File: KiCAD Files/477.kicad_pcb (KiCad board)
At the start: 2 copper layers, 75 parts, among them IC1 W25N01GVSFIG, IC2 W25N01GVSFIG, IC3 W25N01GVSFIG, IC4 W25N01GVSFIG, IC5 AZ1117IH-3.3TRG1, IC6 USBLC6-2SC6, J1 BM06B-SRSS-TBT_LF__SN_, J2 6364372-2, J3 TSW-103-14-S-D, J4 TSW-103-14-S-D, J5 BM07B-SRSS-TB_LF__SN_, J6 BM09B-SRSS-TB_LF__SN_, J7 TSW-105-05-F-S, U1 STM32H7A3RGTx, Y1 ABM8G-48.000MHZ-18-D2Y-T

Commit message: finished file
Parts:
- moved S1 139.7 mm to (218.2, 129.5)
- moved R10 110.3 mm to (225.8, 102.1)
- moved R9 110.3 mm to (225.8, 104.6)
- moved J3 99.9 mm to (250.4, 45.7)
- moved J1 84.6 mm to (173.7, 130.8)
- moved C12 82.6 mm to (166.9, 128.0), turned to 90 degrees
- moved R13 82.1 mm to (166.9, 131.8), turned to -90 degrees
- moved J7 79.6 mm to (195.6, 131.8), turned to 180 degrees
- moved R7 64.4 mm to (226.0, 109.5)
- moved R5 64.4 mm to (226.0, 114.6)
- moved R6 64.4 mm to (226.0, 112.0)
- moved R8 64.4 mm to (226.0, 106.9)
- moved R4 64.4 mm to (226.0, 117.1)
- moved C19 62.6 mm to (230.6, 100.6)
- moved R17 62.5 mm to (233.4, 100.6)
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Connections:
- IC1 pad 7: PA0/CS1 -> PC9/CS1
- IC1 pad 9: PC2/WP1 -> PC7/WP1
- IC2 pad 1: PC7/HOLD2 -> PC2/HOLD2
- IC2 pad 7: PA1/CS2 -> PC10/CS2
- IC3 pad 1: PC9/HOLD3 -> PC4/HOLD3
- IC3 pad 7: PA2/CS3 -> PA3/CS3
- IC3 pad 9: PC4/WP3 -> PC5/WP3
- IC4 pad 1: PC10/HOLD4 -> PA2/HOLD4
- IC4 pad 7: PA3/CS4 -> PA1/CS4
- IC4 pad 9: PC5/WP4 -> PA0/WP4
- U1 pad 10: PC2/WP1 -> PC2/HOLD2
- U1 pad 14: PA0/CS1 -> PA0/WP4
- U1 pad 15: PA1/CS2 -> PA1/CS4
- U1 pad 16: PA2/CS3 -> PA2/HOLD4
- U1 pad 17: PA3/CS4 -> PA3/CS3
- U1 pad 24: PC4/WP3 -> PC4/HOLD3
- U1 pad 25: PC5/WP4 -> PC5/WP3
- U1 pad 38: PC7/HOLD2 -> PC7/WP1
- U1 pad 39: PC9/HOLD3 -> PC9/CS1
- U1 pad 51: PC10/HOLD4 -> PC10/CS2
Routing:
- net PC1/LCD MOSI: track 0.00 -> 104.4 mm, vias 0 -> 2
- net PB10/LCD SCK: track 0.00 -> 47.9 mm
- net PB12/LCD NSS: track 0.00 -> 37.3 mm, vias 0 -> 2
- net PA0/WP4: track 0.00 -> 35.9 mm, vias 0 -> 2
- net PA3/CS3: track 0.00 -> 34.7 mm, vias 0 -> 2
- net PB13/FP TX: track 0.00 -> 30.5 mm, vias 0 -> 2
- net VBAT: track 0.00 -> 28.7 mm, vias 0 -> 6
- net PD2/FP RX: track 0.00 -> 24.7 mm, vias 0 -> 2
- net PC4/HOLD3: track 0.00 -> 21.4 mm, vias 0 -> 2
- net PC7/WP1: track 0.00 -> 18.3 mm, vias 0 -> 4
- net PA1/CS4: track 0.00 -> 16.7 mm
- net PA6/MISO: track 86.7 -> 103.3 mm, vias 2 -> 4
- net PC6/HOLD1: track 0.00 -> 15.6 mm, vias 0 -> 2
- net PA5/SCK: track 79.4 -> 64.2 mm, vias 3 -> 0
- net PA7/MOSI: track 78.2 -> 65.5 mm, vias 3 -> 2
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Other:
- board outline added: 96 x 57.4 mm
- board text added: "Team 20: Encrypted USB Drive Version: 3/5/2025 2:17 AM"
- board text removed: "Team 20: Encrypted USB Drive Version: 3/1/2025 9:25 PM"

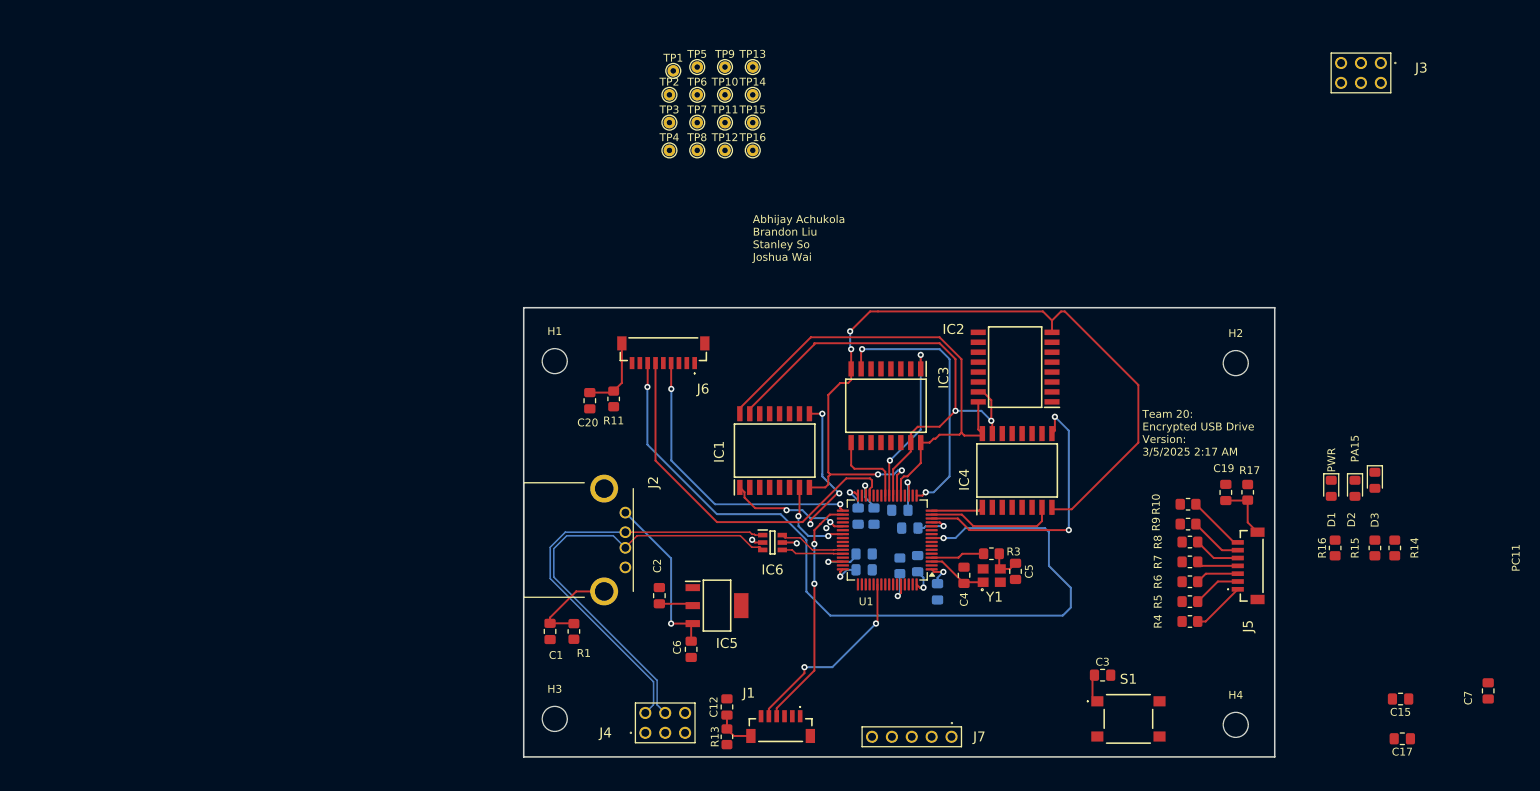
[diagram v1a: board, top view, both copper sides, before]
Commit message: Finalized Signal Routing
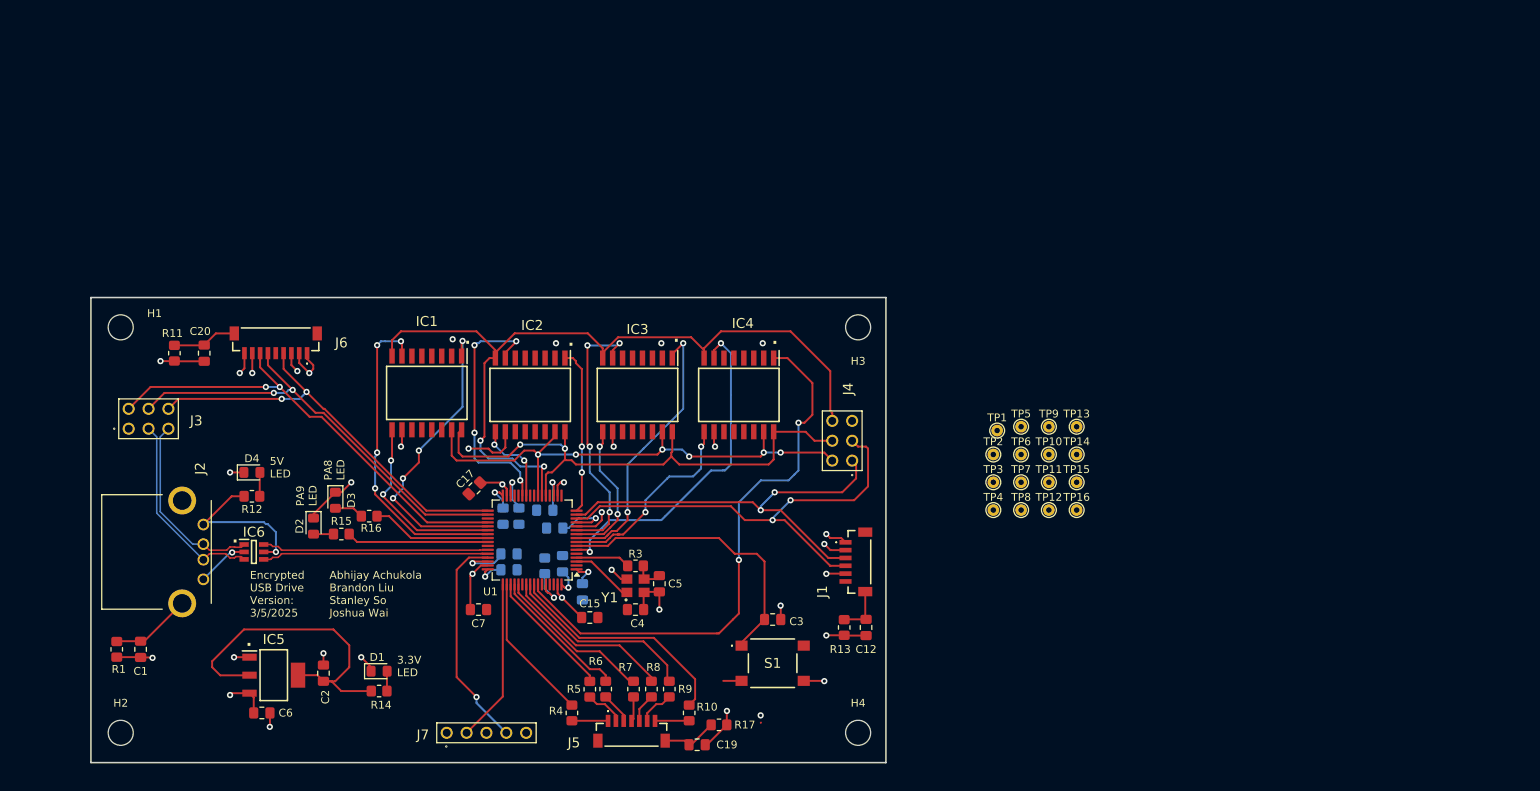
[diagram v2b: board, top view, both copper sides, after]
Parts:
- added D4: LED, LED_SMD:LED_0805_2012Metric_Pad1.15x1.40mm_HandSolder, F.Cu at (106.2, 98.0)
- added R12: 220, Resistor_SMD:R_0805_2012Metric_Pad1.20x1.40mm_HandSolder, F.Cu at (106.2, 101.1)
- moved J3 166.7 mm to (90.4, 92.5), turned to 0 degrees
- moved H2 150.1 mm to (89.4, 131.3)
- moved D2 133.2 mm to (114.0, 104.9)
- moved D3 132.9 mm to (116.8, 101.6)
- moved R15 132.1 mm to (117.6, 105.9), turned to 0 degrees
- moved R14 131.1 mm to (122.4, 126.0), turned to 180 degrees
- moved C7 129.4 mm to (135.1, 115.6), turned to 180 degrees
- moved D1 123.9 mm to (122.4, 123.4), turned to 0 degrees
- moved R16 123.5 mm to (121.2, 103.6), turned to 0 degrees
- moved C17 122.8 mm to (134.6, 100.1), turned to 45 degrees
- moved C15 104.1 mm to (149.4, 116.6)
- moved J5 82.1 mm to (154.7, 131.6), turned to 0 degrees
- moved R4 79.8 mm to (147.1, 128.8), turned to 90 degrees
- moved R5 77.5 mm to (149.4, 125.7), turned to 90 degrees
- moved R6 75.9 mm to (151.4, 125.7), turned to 90 degrees
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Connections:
- IC2 pad 1: PC2/HOLD2 -> PA2/HOLD2
- IC2 pad 7: PC10/CS2 -> PB1/CS2
- IC2 pad 9: PC3/WP2 -> PB0/WP2
- IC3 pad 1: PC4/HOLD3 -> PC1/HOLD3
- IC3 pad 7: PA3/CS3 -> PC3/CS3
- IC3 pad 9: PC5/WP3 -> PC2/WP3
- IC4 pad 1: PA2/HOLD4 -> PB6/HOLD4
- IC4 pad 7: PA1/CS4 -> PH1/CS4
- IC4 pad 9: PA0/WP4 -> PC0/WP4
- J1 pad 2: PC0/Touch Out -> GND
- J1 pad 3: VBAT -> PA1/FP RX
- J1 pad 4: PB13/FP TX -> PA0/FP TX
- J1 pad 5: PD2/FP RX -> VBAT
- J1 pad 6: VBAT -> unconnected-(J1-Pad6)
- J3 pad 2: PA6/MISO -> PB15/LCD MOSI
- J3 pad 3: PB10/LCD SCK -> D+
- J3 pad 4: PA5/SCK -> PB13/LCD SCK
- J3 pad 5: PC1/LCD MOSI -> D-
- J3 pad 6: PA7/MOSI -> PB12/LCD NSS
- J4 pad 1: PC0/Touch Out -> PA1/FP RX
- J4 pad 2: D- -> PA7/MOSI
- J4 pad 3: PB13/FP TX -> PA0/FP TX
- J4 pad 4: D+ -> PA5/SCK
- J4 pad 5: PD2/FP RX -> GND
- J4 pad 6: GND -> PA6/MISO
- J6 pad 6: PB10/LCD SCK -> PB13/LCD SCK
- J6 pad 7: PC1/LCD MOSI -> PB15/LCD MOSI
- R10 pad 1: PB8/KeyC3 -> PB5/KeyC3
- R16 pad 2: PC11/Debug -> PA8/Debug
- R4 pad 2: PB0/KeyR1 -> PA15/KeyR1
- R5 pad 2: PB1/KeyR2 -> PC10/KeyR2
- R6 pad 2: PB2/KeyR3 -> PC11/KeyR3
- R7 pad 1: PB5/KeyR4 -> PC12/KeyR4
- R8 pad 1: PB6/KeyC1 -> PB3/KeyC1
- R9 pad 2: PB7/KeyC2 -> PB4/KeyC2
- TP13 pad 1: PB12/LCD NSS -> unconnected-(TP13-Pad1)
- U1 pad 10: PC2/HOLD2 -> PC2/WP3
- U1 pad 11: PC3/WP2 -> PC3/CS3
- U1 pad 14: PA0/WP4 -> PA0/FP TX
- U1 pad 15: PA1/CS4 -> PA1/FP RX
- U1 pad 16: PA2/HOLD4 -> PA2/HOLD2
- U1 pad 24: PC4/HOLD3 -> unconnected-(U1-PC4-Pad24)
- U1 pad 25: PC5/WP3 -> unconnected-(U1-PC5-Pad25)
- U1 pad 26: PB0/KeyR1 -> PB0/WP2
- U1 pad 27: PB1/KeyR2 -> PB1/CS2
- U1 pad 28: PB2/KeyR3 -> unconnected-(U1-PB2-Pad28)
- U1 pad 29: PB10/LCD SCK -> unconnected-(U1-PB10-Pad29)
- U1 pad 34: PB13/FP TX -> PB13/LCD SCK
- U1 pad 36: unconnected-(U1-PB15-Pad36) -> PB15/LCD MOSI
- U1 pad 40: unconnected-(U1-PA8-Pad40) -> PA8/Debug
- U1 pad 50: unconnected-(U1-PA15-Pad50) -> PA15/KeyR1
- U1 pad 51: PC10/CS2 -> PC10/KeyR2
- U1 pad 52: PC11/Debug -> PC11/KeyR3
- U1 pad 53: unconnected-(U1-PC12-Pad53) -> PC12/KeyR4
- U1 pad 54: PD2/FP RX -> unconnected-(U1-PD2-Pad54)
- U1 pad 55: unconnected-(U1-PB3-Pad55) -> PB3/KeyC1
- U1 pad 56: unconnected-(U1-PB4-Pad56) -> PB4/KeyC2
- U1 pad 57: PB5/KeyR4 -> PB5/KeyC3
- U1 pad 58: PB6/KeyC1 -> PB6/HOLD4
- U1 pad 59: PB7/KeyC2 -> unconnected-(U1-PB7-Pad59)
- U1 pad 6: unconnected-(U1-PH1-Pad6) -> PH1/CS4
- U1 pad 61: PB8/KeyC3 -> unconnected-(U1-PB8-Pad61)
- U1 pad 8: PC0/Touch Out -> PC0/WP4
- U1 pad 9: PC1/LCD MOSI -> PC1/HOLD3
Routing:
- net GND: track 1.49 -> 108.7 mm, vias 1 -> 28
- net PC1/LCD MOSI: track 104.4 -> 0.00 mm, vias 2 -> 0
- net PB6/HOLD4: track 0.00 -> 72.0 mm, vias 0 -> 2
- net PB15/LCD MOSI: track 0.00 -> 60.4 mm, vias 0 -> 2
- net PA0/FP TX: track 0.00 -> 59.6 mm, vias 0 -> 2
- net PB13/LCD SCK: track 0.00 -> 57.0 mm, vias 0 -> 2
- net PA1/FP RX: track 0.00 -> 54.6 mm, vias 0 -> 2
- net PB10/LCD SCK: track 47.9 -> 0.00 mm
- net VBAT: track 28.7 -> 75.1 mm, vias 6 -> 12
- net PH1/CS4: track 0.00 -> 43.6 mm, vias 0 -> 2
- net PA0/WP4: track 35.9 -> 0.00 mm, vias 2 -> 0
- net PC1/HOLD3: track 0.00 -> 35.5 mm, vias 0 -> 2
- net PC3/CS3: track 0.00 -> 35.0 mm, vias 0 -> 4
- net nRST: track 2.97 -> 37.8 mm
- net PA3/CS3: track 34.7 -> 0.00 mm, vias 2 -> 0
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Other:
- board size 96 x 57.4 mm -> 101.6 x 59.4 mm
- board text added: "."
- board text added: "3.3V LED"
- board text added: "5V LED"
- board text added: "Encrypted USB Drive Version: 3/5/2025"
- board text added: "PA8 LED"
- board text added: "PA9 LED"
- board text removed: "PA15"
- board text removed: "PC11"
- board text removed: "PWR"
- board text removed: "Team 20: Encrypted USB Drive Version: 3/5/2025 2:17 AM"

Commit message: finalized 99% of pcb
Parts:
- removed TP13, TP15, TP16: TestPoint, TestPoint:TestPoint_THTPad_D1.5mm_Drill0.7mm
- TP1, TP10, TP11, TP12, TP2, TP3, TP4, TP5, TP6, TP7, TP8, TP9: footprint TestPoint:TestPoint_THTPad_D1.5mm_Drill0.7mm -> TestPoint:TestPoint_THTPad_D1.0mm_Drill0.5mm
- moved TP12 86.3 mm to (125.2, 78.5)
- moved TP1 76.0 mm to (125.5, 96.8)
- moved TP5 72.7 mm to (133.1, 78.5)
- moved TP11 71.3 mm to (139.7, 78.7)
- moved TP2 62.8 mm to (138.2, 98.0)
- moved TP6 60.6 mm to (146.3, 78.7)
- moved TP10 58.0 mm to (152.4, 79.2)
- moved TP14 54.6 mm to (164.3, 123.2)
- moved TP7 48.4 mm to (160.5, 79.0)
- moved TP3 48.0 mm to (152.9, 98.3)
- moved TP9 45.4 mm to (164.6, 79.0)
- moved TP4 40.7 mm to (160.3, 100.1)
- moved TP8 40.0 mm to (172.7, 78.5)
- moved J2 1.27 mm to (98.7, 104.6)
- moved R3 0.76 mm to (155.2, 109.2)
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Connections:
- TP1 pad 1: PC2/WP1 -> PC7/WP1
- TP10 pad 1: PA2/CS3 -> PC3/CS3
- TP11 pad 1: PA1/CS2 -> PB1/CS2
- TP12 pad 1: PA0/CS1 -> PC9/CS1
- TP14 pad 1: PB8/KeyC3 -> PB5/KeyC3
- TP2 pad 1: PC3/WP2 -> PB0/WP2
- TP3 pad 1: PC4/WP3 -> PC2/WP3
- TP4 pad 1: PC5/WP4 -> PC0/WP4
- TP6 pad 1: PC7/HOLD2 -> PA2/HOLD2
- TP7 pad 1: PC9/HOLD3 -> PC1/HOLD3
- TP8 pad 1: PC10/HOLD4 -> PB6/HOLD4
- TP9 pad 1: PA3/CS4 -> PH1/CS4
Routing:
- net VBAT: track 75.1 -> 351.9 mm, vias 12 -> 17
- net +5V: track 31.4 -> 107.9 mm
- net nRST: track 37.8 -> 69.9 mm, vias 0 -> 1
- net GND: track 108.7 -> 126.6 mm, vias 28 -> 30
- net D-: track 24.1 -> 29.6 mm
- net PB6/HOLD4: track 72.0 -> 77.0 mm, vias 2 -> 3
- net PA2/HOLD2: track 21.5 -> 26.3 mm, vias 2 -> 3
- net D+: track 25.6 -> 30.3 mm
- net PB1/CS2: track 32.4 -> 36.0 mm
- net PB0/WP2: track 10.9 -> 14.4 mm
- net PC9/CS1: track 41.1 -> 44.5 mm
- net PC3/CS3: track 35.0 -> 38.3 mm
- net PH1/CS4: track 43.6 -> 46.8 mm
- net PC1/HOLD3: track 35.5 -> 38.3 mm
- net PC6/HOLD1: track 39.4 -> 42.1 mm
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- added copper zone on B.Cu, net GND
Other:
- board text added: "Encrypted USB Drive Version: 3/6/2025"
- board text removed: "Encrypted USB Drive Version: 3/5/2025"

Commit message: updated files with 3d models
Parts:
- TP14: footprint TestPoint:TestPoint_THTPad_D1.5mm_Drill0.7mm -> TestPoint:TestPoint_THTPad_D1.0mm_Drill0.5mm
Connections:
- net Net-(U1-BOOT0) renamed /Microcontroller Circuitry/BOOT0
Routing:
- net nRST: track 69.9 -> 70.9 mm
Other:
- board text removed: "."

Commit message: finished schematic and pcb
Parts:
- moved J2 3.21 mm to (95.5, 104.7)
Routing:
- net +5V: track 107.9 -> 116.5 mm
- net D-: track 29.6 -> 36.3 mm
- net D+: track 30.3 -> 37.0 mm
- net GND: track 126.6 -> 120.1 mm
- net Net-(C1-Pad1): track 10.1 -> 8.92 mm
- net PA6/MISO: track 103.1 -> 102.0 mm

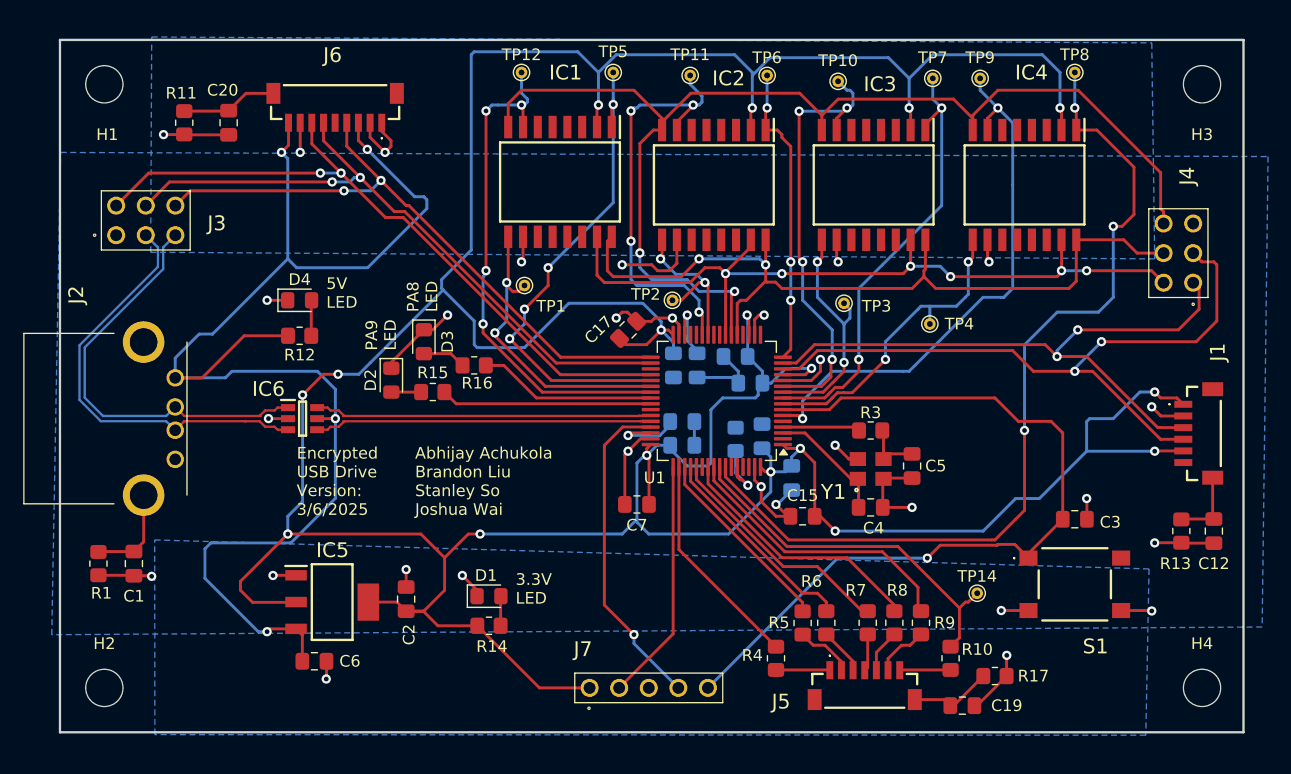
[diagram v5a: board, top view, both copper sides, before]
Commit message: rounded edges
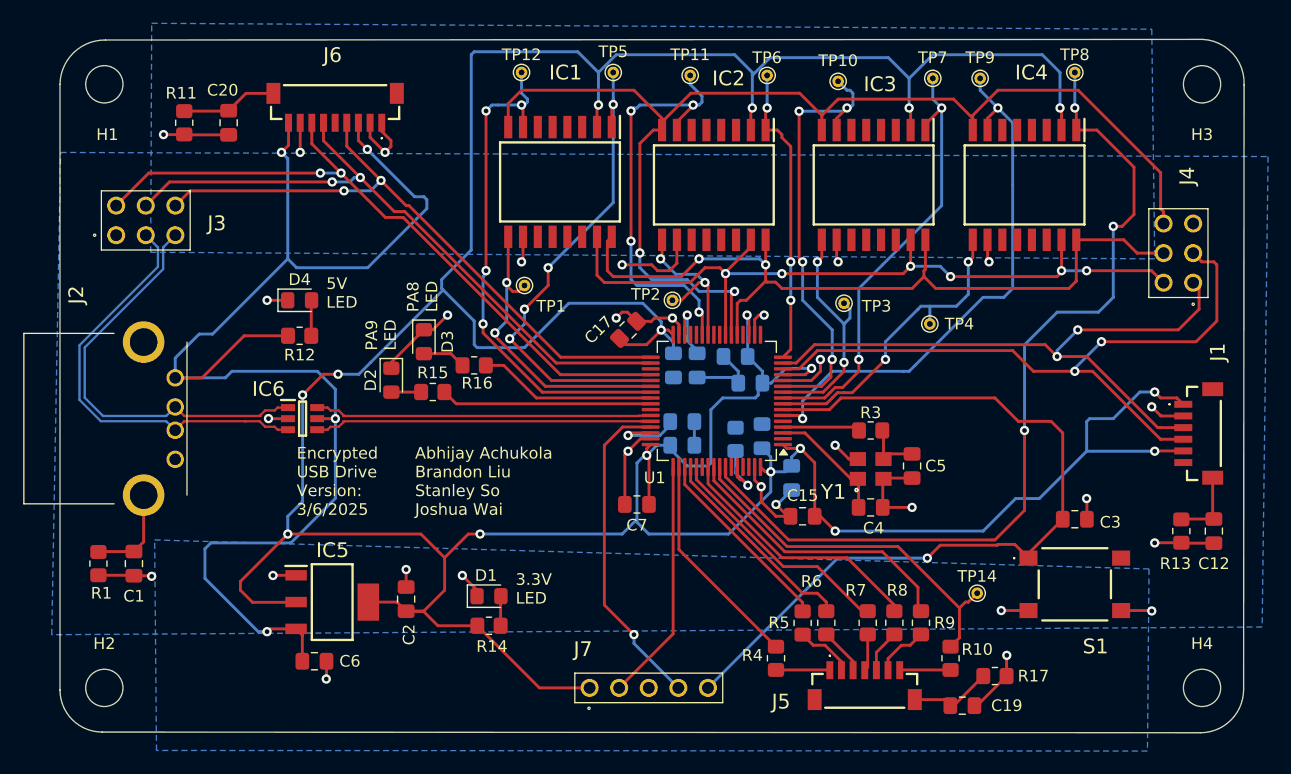
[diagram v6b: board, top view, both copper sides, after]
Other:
- board size 101.6 x 59.4 mm -> 101.7 x 59.5 mm
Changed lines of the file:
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@@
 		)
 	)
-	(gr_rect
-		(start 85.598 75.692)
-		(end 187.198 135.128)
+	(gr_arc
+		(start 89.22269 135.11063)
+		(mid 86.663558 134.055599)
+		(end 85.6 131.5)
 		(stroke
-			(width 0.2)
+			(width 0.1)
+			(type default)
+		)
+		(layer "Edge.Cuts")
+	)
+	(gr_line
+		(start 85.6 79.5)
+		(end 85.6 131.5)
+		(stroke
+			(width 0.1)
+			(type default)
+		)
+		(layer "Edge.Cuts")
+	)
+	(gr_arc
+		(start 187.21063 131.44731)
+		(mid 186.12631 134.077152)
+		(end 183.5 135.17)
+		(stroke
+			(width 0.1)
+			(type default)
+		)
+		(layer "Edge.Cuts")
+	)
+	(gr_line
+		(start 183.69731 75.64669)
+		(end 89.51063 75.7)
+		(stroke
+			(width 0.1)
+			(type default)
+		)
+		(layer "Edge.Cuts")
+	)
+	(gr_line
+		(start 187.21063 131.44731)
+		(end 187.25 79.55732)
+		(stroke
+			(width 0.1)
+			(type default)
+		)
+		(layer "Edge.Cuts")
+	)
+	(gr_line
+		(start 89.22269 135.11063)
+		(end 183.5 135.17)
+		(stroke
+			(width 0.1)
+			(type default)
+		)
+		(layer "Edge.Cuts")
+	)
+	(gr_arc
+		(start 183.69731 75.64669)
+		(mid 186.283573 76.866219)
+		(end 187.25 79.55732)
+		(stroke
+			(width 0.1)
+			(type default)
+		)
+		(layer "Edge.Cuts")
+	)
+	(gr_arc
+		(start 85.6 79.5)
+		(mid 86.768308 76.790081)
+		(end 89.51063 75.7)
+		(stroke
+			(width 0.1)
 			(type default)
 		)
-		(fill none)
 		(layer "Edge.Cuts")
 	)
@@
 		(polygon
 			(pts
-				(xy 93.472 75.438) (xy 179.324 75.946) (xy 179.578 94.488) (xy 93.388474 93.918613)
+				(xy 93.472 74.264655) (xy 179.324 74.772655) (xy 179.578 94.488) (xy 93.388474 93.918613)
 			)
 		)
@@
 		(polygon
 			(pts
-				(xy 93.726 118.618) (xy 179.090877 121.105803) (xy 178.816 135.382) (xy 93.746877 135.329803)
+				(xy 93.726 118.618) (xy 179.090877 121.105803) (xy 178.954655 136.741685) (xy 93.885532 136.689488)
 			)
 		)

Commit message: updated pcb
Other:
- board text added: "Team 20"
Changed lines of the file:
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@@
+		)
+	)
+	(gr_text "Team 20"
+		(at 112.5 134 0)
+		(layer "F.SilkS")
+		(effects
+			(font
+				(size 1 1)
+				(thickness 0.1875)
+			)
+			(justify left bottom)
 		)
 	)
